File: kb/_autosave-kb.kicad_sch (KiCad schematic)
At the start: 110 parts, among them J1 Conn_01x04_MountingPin, SW1 SW_Push, SW10 SW_Push, SW11 SW_Push, SW12 SW_Push, SW13 SW_Push, SW14 SW_Push, SW15 SW_Push, SW16 SW_Push, SW17 SW_Push, SW18 SW_Push, SW19 SW_Push, SW2 SW_Push, SW20 SW_Push, SW21 SW_Push, SW22 SW_Push, SW23 SW_Push, SW24 SW_Push, SW25 SW_Push, SW26 SW_Push, SW27 SW_Push, SW28 SW_Push, SW29 SW_Push, SW3 SW_Push, SW30 SW_Push, SW31 SW_Push, SW32 SW_Push, SW33 SW_Push, SW34 SW_Push, SW35 SW_Push, SW36 SW_Push, SW37 SW_Push, SW38 SW_Push, SW39 SW_Push, SW4 SW_Push, SW40 SW_Push, SW41 SW_Push, SW42 SW_Push, SW43 SW_Push, SW44 SW_Push, SW45 SW_Push, SW46 SW_Push, SW47 SW_Push, SW48 SW_Push, SW5 SW_Push, SW6 SW_Push, SW7 SW_Push, SW8 SW_Push, SW9 SW_Push, U2 STM32G474CETx, U4 XC6206PxxxMR

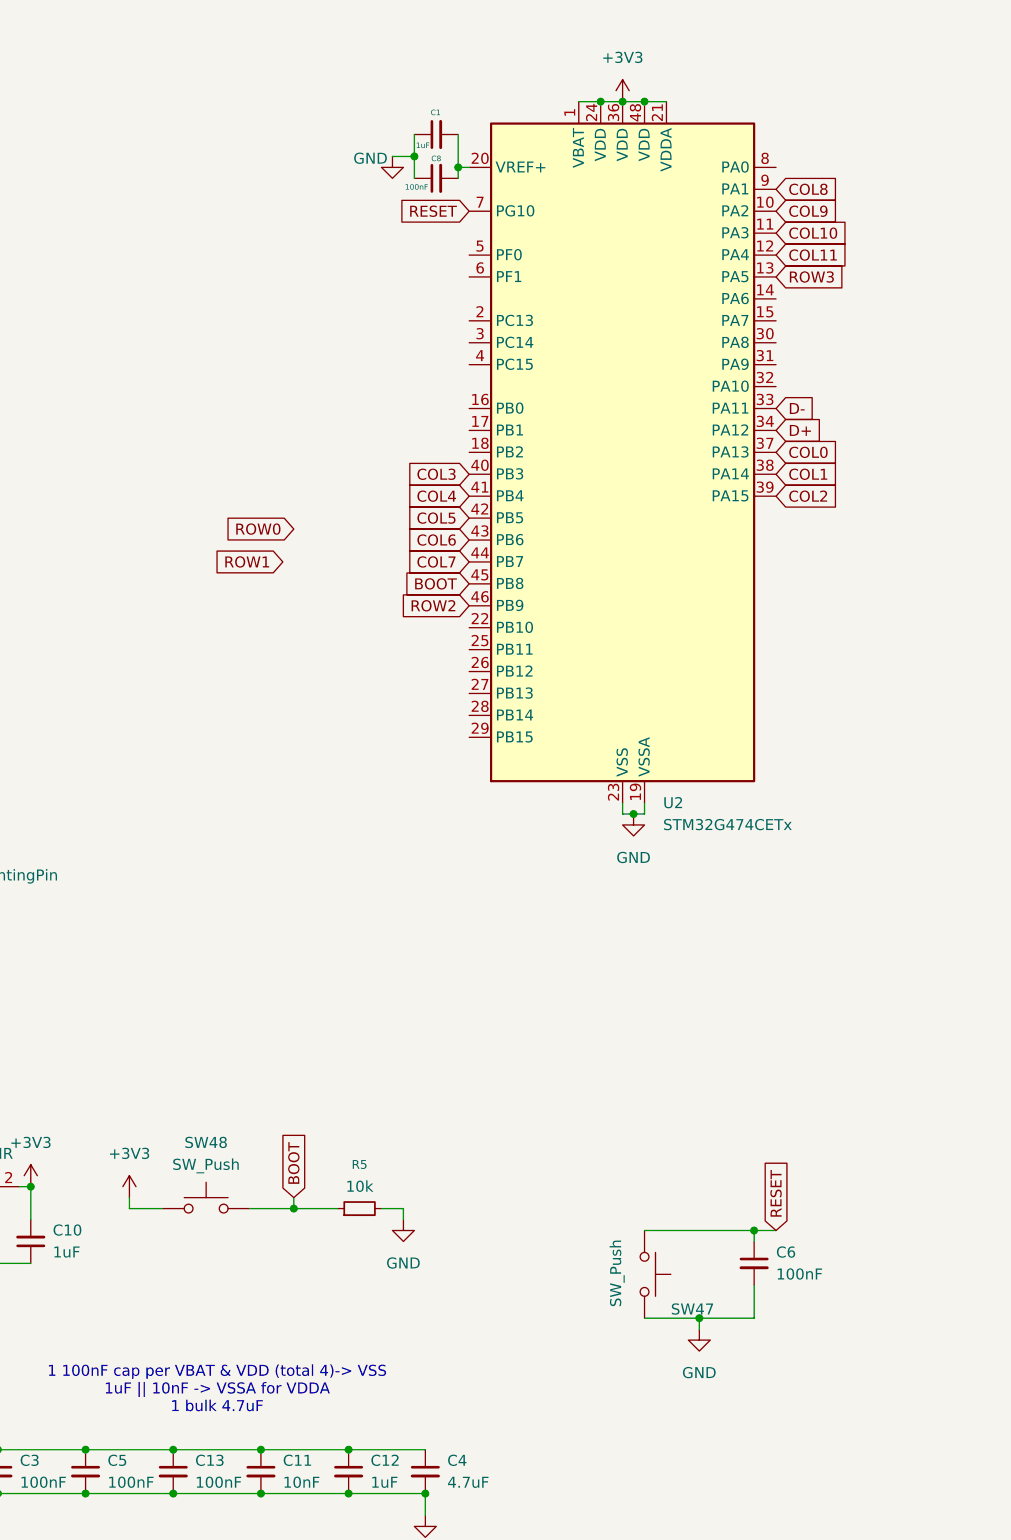
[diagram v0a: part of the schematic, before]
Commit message: Added NSRT, Fixed Pins
Fixed boot pin and reset pin assignments, rerouted accordingly
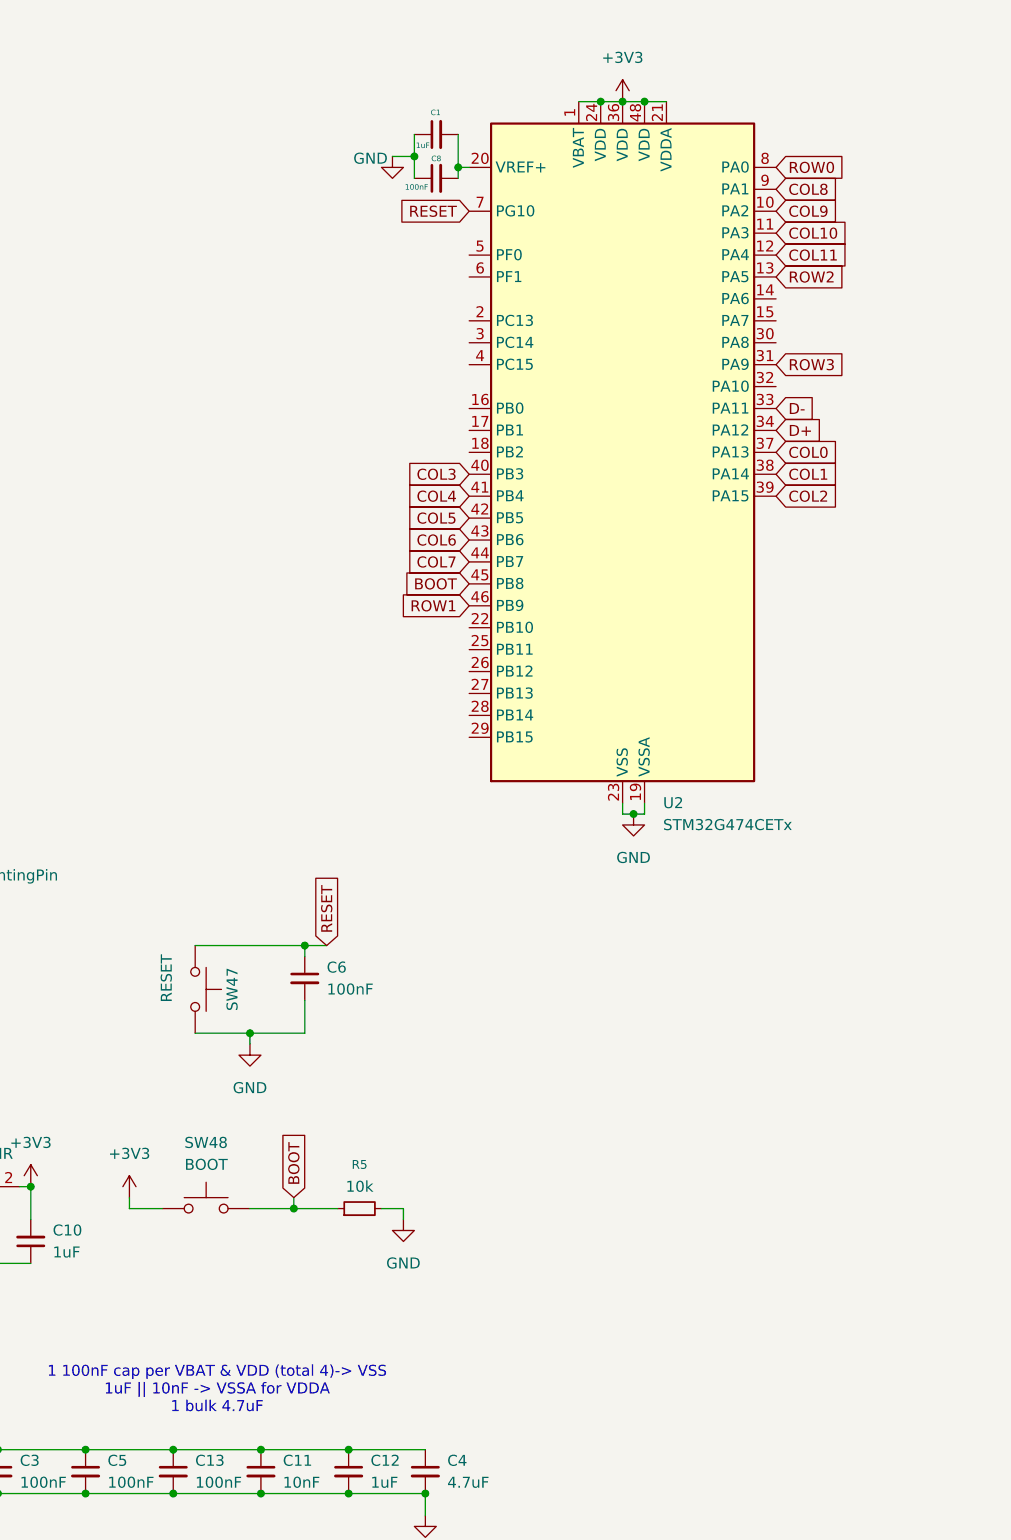
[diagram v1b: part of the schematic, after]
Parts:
- SW47: value SW_Push -> RESET
- SW48: value SW_Push -> BOOT
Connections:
- net ROW0: now also U2.8 (PA0)
- net ROW1: now also U2.46 (PB9)
- net ROW2: now also U2.13 (PA5); no longer U2.46 (PB9)
- net ROW3: now also U2.31 (PA9); no longer U2.13 (PA5)
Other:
- moved on the sheet: C6, SW47
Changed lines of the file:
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@@
 	)
 	(junction
-		(at 114.3 195.58)
+		(at 62.23 162.56)
 		(diameter 0)
 		(color 0 0 0 0)
@@
 	)
 	(junction
-		(at 120.65 185.42)
+		(at 68.58 152.4)
 		(diameter 0)
 		(color 0 0 0 0)
@@
 	(wire
 		(pts
-			(xy 114.3 195.58) (xy 114.3 196.85)
+			(xy 62.23 162.56) (xy 62.23 163.83)
 		)
 		(stroke
@@
 	(wire
 		(pts
-			(xy 120.65 195.58) (xy 114.3 195.58)
+			(xy 68.58 162.56) (xy 62.23 162.56)
 		)
 		(stroke
@@
 	(wire
 		(pts
-			(xy 107.95 185.42) (xy 120.65 185.42)
+			(xy 55.88 152.4) (xy 68.58 152.4)
 		)
 		(stroke
@@
 	(wire
 		(pts
-			(xy 120.65 185.42) (xy 123.19 185.42)
+			(xy 68.58 152.4) (xy 71.12 152.4)
 		)
 		(stroke
@@
 	(wire
 		(pts
-			(xy 120.65 191.77) (xy 120.65 195.58)
+			(xy 68.58 158.75) (xy 68.58 162.56)
 		)
 		(stroke
@@
 	(wire
 		(pts
-			(xy 120.65 186.69) (xy 120.65 185.42)
+			(xy 68.58 153.67) (xy 68.58 152.4)
 		)
 		(stroke
@@
 	(wire
 		(pts
-			(xy 107.95 195.58) (xy 114.3 195.58)
+			(xy 55.88 162.56) (xy 62.23 162.56)
 		)
 		(stroke
@@
 	(global_label "ROW0"
 		(shape input)
-		(at 67.31 104.14 180)
+		(at 123.19 62.23 0)
 		(fields_autoplaced yes)
 		(effects
@@
 				(size 1.27 1.27)
 			)
-			(justify right)
+			(justify left)
 		)
 		(property "Intersheetrefs" "${INTERSHEET_REFS}"
-			(at 59.0634 104.14 0)
+			(at 131.4366 62.23 0)
 			(effects
 				(font
 					(size 1.27 1.27)
 				)
-				(justify right)
+				(justify left)
 				(hide yes)
 			)
@@
 	(global_label "ROW1"
 		(shape input)
-		(at 66.04 107.95 180)
+		(at 87.63 113.03 180)
 		(fields_autoplaced yes)
 		(effects
@@
 		)
 		(property "Intersheetrefs" "${INTERSHEET_REFS}"
-			(at 57.7934 107.95 0)
+			(at 79.3834 113.03 0)
 			(effects
 				(font
@@
 	(global_label "ROW2"
 		(shape input)
-		(at 87.63 113.03 180)
+		(at 123.19 74.93 0)
 		(fields_autoplaced yes)
 		(effects
@@
 				(size 1.27 1.27)
 			)
-			(justify right)
+			(justify left)
 		)
 		(property "Intersheetrefs" "${INTERSHEET_REFS}"
-			(at 79.3834 113.03 0)
+			(at 131.4366 74.93 0)
 			(effects
 				(font
 					(size 1.27 1.27)
 				)
-				(justify right)
+				(justify left)
 				(hide yes)
 			)
@@
 	(global_label "ROW3"
 		(shape input)
-		(at 123.19 74.93 0)
+		(at 123.19 85.09 0)
 		(fields_autoplaced yes)
 		(effects
@@
 		)
 		(property "Intersheetrefs" "${INTERSHEET_REFS}"
-			(at 131.4366 74.93 0)
+			(at 131.4366 85.09 0)
 			(effects
 				(font
@@
 	(global_label "RESET"
 		(shape input)
-		(at 123.19 185.42 90)
+		(at 71.12 152.4 90)
 		(fields_autoplaced yes)
 		(effects
@@
 		)
 		(property "Intersheetrefs" "${INTERSHEET_REFS}"
-			(at 123.19 176.6897 90)
+			(at 71.12 143.6697 90)
 			(effects
 				(font
@@
 			)
 		)
-		(property "Value" "SW_Push"
+		(property "Value" "BOOT"
 			(at 57.15 177.8 0)
 			(effects
@@
 	(symbol
 		(lib_id "Switch:SW_Push")
-		(at 107.95 190.5 270)
+		(at 55.88 157.48 270)
 		(unit 1)
 		(exclude_from_sim no)
@@
 		(dnp no)
 		(property "Reference" "SW47"
-			(at 110.998 194.564 90)
+			(at 60.198 154.94 0)
 			(effects
 				(font
@@
 			)
 		)
-		(property "Value" "SW_Push"
-			(at 104.648 186.436 0)
+		(property "Value" "RESET"
+			(at 52.578 153.416 0)
 			(effects
 				(font
@@
 		)
 		(property "Footprint" "Button_Switch_SMD:SW_SPST_SKQG_WithStem"
-			(at 113.03 190.5 0)
+			(at 60.96 157.48 0)
 			(effects
 				(font
@@
 		)
 		(property "Datasheet" "~"
-			(at 113.03 190.5 0)
+			(at 60.96 157.48 0)
 			(effects
 				(font
@@
 		)
 		(property "Description" "Push button switch, generic, two pins"
-			(at 107.95 190.5 0)
+			(at 55.88 157.48 0)
 			(effects
 				(font
@@
 	(symbol
 		(lib_id "Device:C_Small")
-		(at 120.65 189.23 0)
+		(at 68.58 156.21 0)
 		(unit 1)
 		(exclude_from_sim no)
@@
 		(fields_autoplaced yes)
 		(property "Reference" "C6"
-			(at 123.19 187.9662 0)
+			(at 71.12 154.9462 0)
 			(effects
 				(font
@@
 		)
 		(property "Value" "100nF"
-			(at 123.19 190.5062 0)
+			(at 71.12 157.4862 0)
 			(effects
 				(font
@@
 		)
 		(property "Footprint" "Capacitor_SMD:C_0805_2012Metric"
-			(at 120.65 189.23 0)
+			(at 68.58 156.21 0)
 			(effects
 				(font
@@
 		)
 		(property "Datasheet" "~"
-			(at 120.65 189.23 0)
+			(at 68.58 156.21 0)
 			(effects
 				(font
@@
 		)
 		(property "Description" "Unpolarized capacitor, small symbol"
-			(at 120.65 189.23 0)
+			(at 68.58 156.21 0)
 			(effects
 				(font
@@
 	(symbol
 		(lib_id "power:GND")
-		(at 114.3 196.85 0)
+		(at 62.23 163.83 0)
 		(unit 1)
 		(exclude_from_sim no)
@@
 		(fields_autoplaced yes)
 		(property "Reference" "#PWR04"
-			(at 114.3 203.2 0)
+			(at 62.23 170.18 0)
 			(effects
 				(font
@@
 		)
 		(property "Value" "GND"
-			(at 114.3 201.93 0)
+			(at 62.23 168.91 0)
 			(effects
 				(font
@@
 		)
 		(property "Footprint" ""
-			(at 114.3 196.85 0)
+			(at 62.23 163.83 0)
 			(effects
 				(font
@@
 		)
 		(property "Datasheet" ""
-			(at 114.3 196.85 0)
+			(at 62.23 163.83 0)
 			(effects
 				(font
@@
 		)
 		(property "Description" "Power symbol creates a global label with name \"GND\" , ground"
-			(at 114.3 196.85 0)
+			(at 62.23 163.83 0)
 			(effects
 				(font

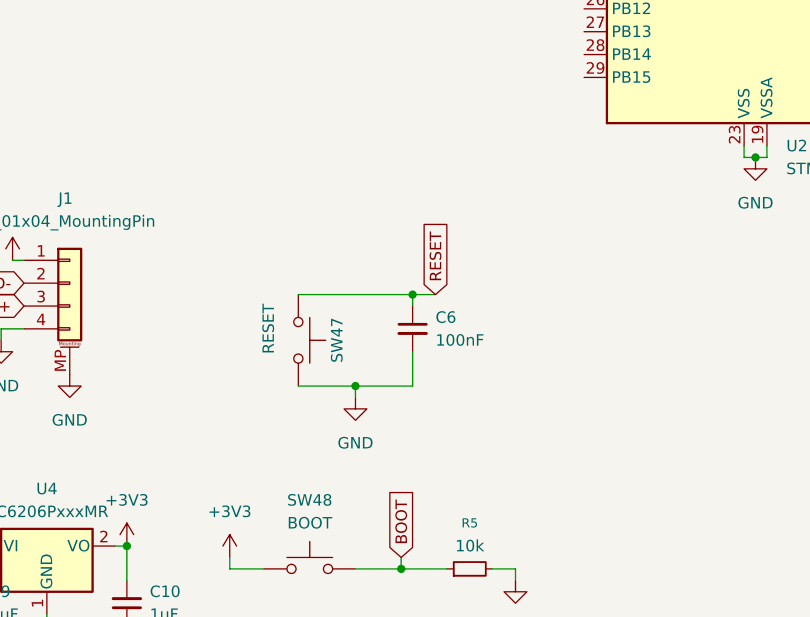
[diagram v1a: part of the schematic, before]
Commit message: Shrunk passive footprints
Switched footprint of passives from 0805  to 0402 and rewired accordingly
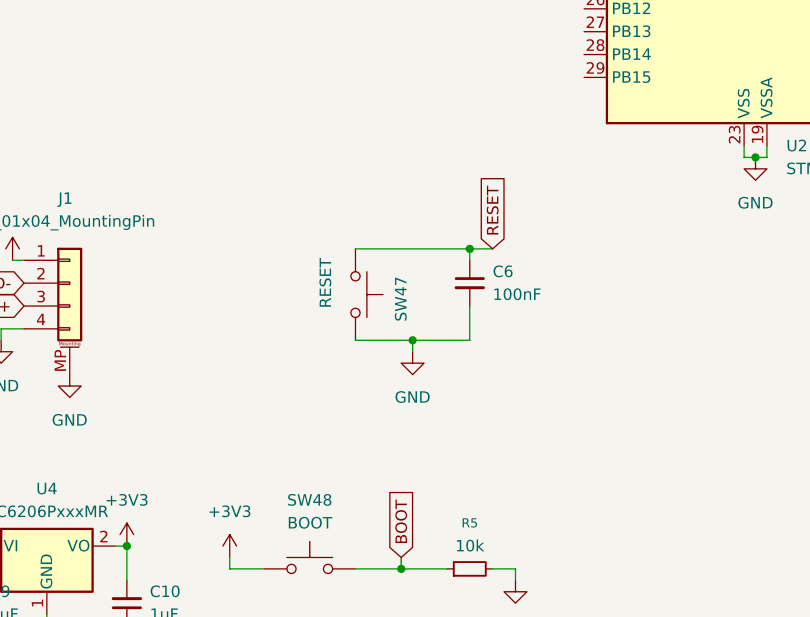
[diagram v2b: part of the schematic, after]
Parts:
- C1, C10, C11, C12, C13, C2, C3, C4, C5, C6, C8, C9: footprint Capacitor_SMD:C_0805_2012Metric -> Capacitor_SMD:C_0402_1005Metric
- R5: footprint Resistor_SMD:R_0805_2012Metric -> Resistor_SMD:R_0402_1005Metric
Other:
- moved on the sheet: C6, SW47
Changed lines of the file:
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@@
 	)
 	(junction
-		(at 62.23 162.56)
+		(at 68.58 157.48)
 		(diameter 0)
 		(color 0 0 0 0)
@@
 	)
 	(junction
-		(at 68.58 152.4)
+		(at 74.93 147.32)
 		(diameter 0)
 		(color 0 0 0 0)
@@
 	(wire
 		(pts
-			(xy 62.23 162.56) (xy 62.23 163.83)
+			(xy 68.58 157.48) (xy 68.58 158.75)
 		)
 		(stroke
@@
 	(wire
 		(pts
-			(xy 68.58 162.56) (xy 62.23 162.56)
+			(xy 74.93 157.48) (xy 68.58 157.48)
 		)
 		(stroke
@@
 	(wire
 		(pts
-			(xy 55.88 152.4) (xy 68.58 152.4)
+			(xy 62.23 147.32) (xy 74.93 147.32)
 		)
 		(stroke
@@
 	(wire
 		(pts
-			(xy 68.58 152.4) (xy 71.12 152.4)
+			(xy 74.93 147.32) (xy 77.47 147.32)
 		)
 		(stroke
@@
 	(wire
 		(pts
-			(xy 68.58 158.75) (xy 68.58 162.56)
+			(xy 74.93 153.67) (xy 74.93 157.48)
 		)
 		(stroke
@@
 	(wire
 		(pts
-			(xy 68.58 153.67) (xy 68.58 152.4)
+			(xy 74.93 148.59) (xy 74.93 147.32)
 		)
 		(stroke
@@
 	(wire
 		(pts
-			(xy 55.88 162.56) (xy 62.23 162.56)
+			(xy 62.23 157.48) (xy 68.58 157.48)
 		)
 		(stroke
@@
 	(global_label "RESET"
 		(shape input)
-		(at 71.12 152.4 90)
+		(at 77.47 147.32 90)
 		(fields_autoplaced yes)
 		(effects
@@
 		)
 		(property "Intersheetrefs" "${INTERSHEET_REFS}"
-			(at 71.12 143.6697 90)
+			(at 77.47 138.5897 90)
 			(effects
 				(font
@@
 			)
 		)
-		(property "Footprint" "Capacitor_SMD:C_0805_2012Metric"
+		(property "Footprint" "Capacitor_SMD:C_0402_1005Metric"
 			(at 36.83 186.69 0)
 			(effects
@@
 			)
 		)
-		(property "Footprint" "Capacitor_SMD:C_0805_2012Metric"
+		(property "Footprint" "Capacitor_SMD:C_0402_1005Metric"
 			(at 83.82 63.5 0)
 			(effects
@@
 	(symbol
 		(lib_id "Switch:SW_Push")
-		(at 55.88 157.48 270)
+		(at 62.23 152.4 270)
 		(unit 1)
 		(exclude_from_sim no)
@@
 		(dnp no)
 		(property "Reference" "SW47"
-			(at 60.198 154.94 0)
+			(at 67.31 150.368 0)
 			(effects
 				(font
@@
 		)
 		(property "Value" "RESET"
-			(at 52.578 153.416 0)
+			(at 58.928 148.336 0)
 			(effects
 				(font
@@
 		)
 		(property "Footprint" "Button_Switch_SMD:SW_SPST_SKQG_WithStem"
-			(at 60.96 157.48 0)
+			(at 67.31 152.4 0)
 			(effects
 				(font
@@
 		)
 		(property "Datasheet" "~"
-			(at 60.96 157.48 0)
+			(at 67.31 152.4 0)
 			(effects
 				(font
@@
 		)
 		(property "Description" "Push button switch, generic, two pins"
-			(at 55.88 157.48 0)
+			(at 62.23 152.4 0)
 			(effects
 				(font
@@
 			)
 		)
-		(property "Footprint" "Capacitor_SMD:C_0805_2012Metric"
+		(property "Footprint" "Capacitor_SMD:C_0402_1005Metric"
 			(at 82.55 213.36 0)
 			(effects
@@
 			)
 		)
-		(property "Footprint" "Capacitor_SMD:C_0805_2012Metric"
+		(property "Footprint" "Capacitor_SMD:C_0402_1005Metric"
 			(at 19.05 186.69 0)
 			(effects
@@
 	(symbol
 		(lib_id "Device:C_Small")
-		(at 68.58 156.21 0)
+		(at 74.93 151.13 0)
 		(unit 1)
 		(exclude_from_sim no)
@@
 		(fields_autoplaced yes)
 		(property "Reference" "C6"
-			(at 71.12 154.9462 0)
+			(at 77.47 149.8662 0)
 			(effects
 				(font
@@
 		)
 		(property "Value" "100nF"
-			(at 71.12 157.4862 0)
+			(at 77.47 152.4062 0)
 			(effects
 				(font
@@
 			)
 		)
-		(property "Footprint" "Capacitor_SMD:C_0805_2012Metric"
-			(at 68.58 156.21 0)
+		(property "Footprint" "Capacitor_SMD:C_0402_1005Metric"
+			(at 74.93 151.13 0)
 			(effects
 				(font
@@
 		)
 		(property "Datasheet" "~"
-			(at 68.58 156.21 0)
+			(at 74.93 151.13 0)
 			(effects
 				(font
@@
 		)
 		(property "Description" "Unpolarized capacitor, small symbol"
-			(at 68.58 156.21 0)
+			(at 74.93 151.13 0)
 			(effects
 				(font
@@
 			)
 		)
-		(property "Footprint" "Capacitor_SMD:C_0805_2012Metric"
+		(property "Footprint" "Capacitor_SMD:C_0402_1005Metric"
 			(at 83.82 58.42 0)
 			(effects
@@
 			)
 		)
-		(property "Footprint" "Capacitor_SMD:C_0805_2012Metric"
+		(property "Footprint" "Capacitor_SMD:C_0402_1005Metric"
 			(at 53.34 213.36 0)
 			(effects
@@
 			)
 		)
-		(property "Footprint" "Resistor_SMD:R_0805_2012Metric"
+		(property "Footprint" "Resistor_SMD:R_0402_1005Metric"
 			(at 74.93 182.88 0)
 			(effects
@@
 	(symbol
 		(lib_id "power:GND")
-		(at 62.23 163.83 0)
+		(at 68.58 158.75 0)
 		(unit 1)
 		(exclude_from_sim no)
@@
 		(fields_autoplaced yes)
 		(property "Reference" "#PWR04"
-			(at 62.23 170.18 0)
+			(at 68.58 165.1 0)
 			(effects
 				(font
@@
 		)
 		(property "Value" "GND"
-			(at 62.23 168.91 0)
+			(at 68.58 163.83 0)
 			(effects
 				(font
@@
 		)
 		(property "Footprint" ""
-			(at 62.23 163.83 0)
+			(at 68.58 158.75 0)
 			(effects
 				(font
@@
 		)
 		(property "Datasheet" ""
-			(at 62.23 163.83 0)
+			(at 68.58 158.75 0)
 			(effects
 				(font
@@
 		)
 		(property "Description" "Power symbol creates a global label with name \"GND\" , ground"
-			(at 62.23 163.83 0)
+			(at 68.58 158.75 0)
 			(effects
 				(font
@@
 			)
 		)
-		(property "Footprint" "Capacitor_SMD:C_0805_2012Metric"
+		(property "Footprint" "Capacitor_SMD:C_0402_1005Metric"
 			(at 22.86 213.36 0)
 			(effects
@@
 			)
 		)
-		(property "Footprint" "Capacitor_SMD:C_0805_2012Metric"
+		(property "Footprint" "Capacitor_SMD:C_0402_1005Metric"
 			(at 43.18 213.36 0)
 			(effects
@@
 			)
 		)
-		(property "Footprint" "Capacitor_SMD:C_0805_2012Metric"
+		(property "Footprint" "Capacitor_SMD:C_0402_1005Metric"
 			(at 73.66 213.36 0)
 			(effects
@@
 			)
 		)
-		(property "Footprint" "Capacitor_SMD:C_0805_2012Metric"
+		(property "Footprint" "Capacitor_SMD:C_0402_1005Metric"
 			(at 33.02 213.36 0)
 			(effects
@@
 			)
 		)
-		(property "Footprint" "Capacitor_SMD:C_0805_2012Metric"
+		(property "Footprint" "Capacitor_SMD:C_0402_1005Metric"
 			(at 63.5 213.36 0)
 			(effects
